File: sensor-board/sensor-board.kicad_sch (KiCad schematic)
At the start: 7 parts, among them U1 NE5532

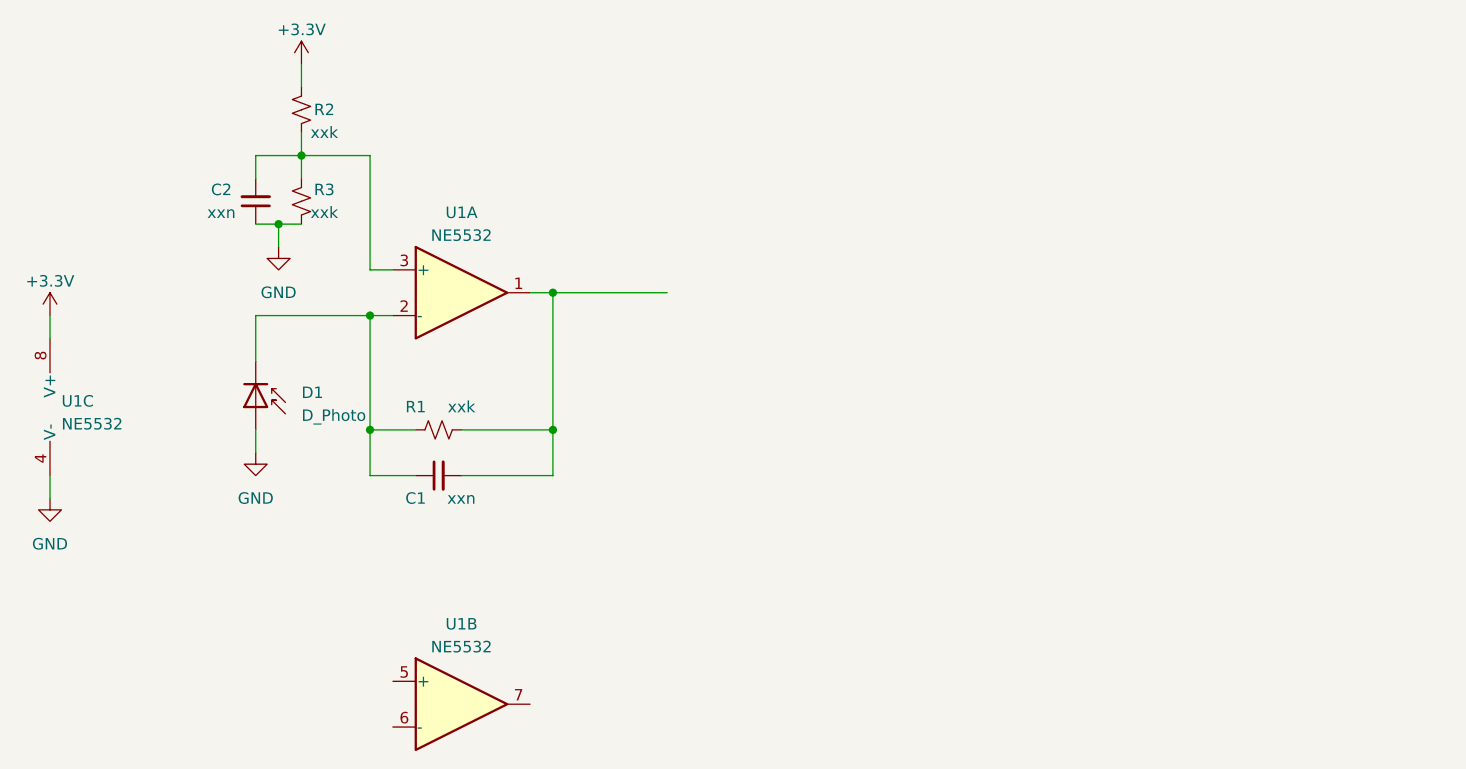
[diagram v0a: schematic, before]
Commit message: Updated sensor board
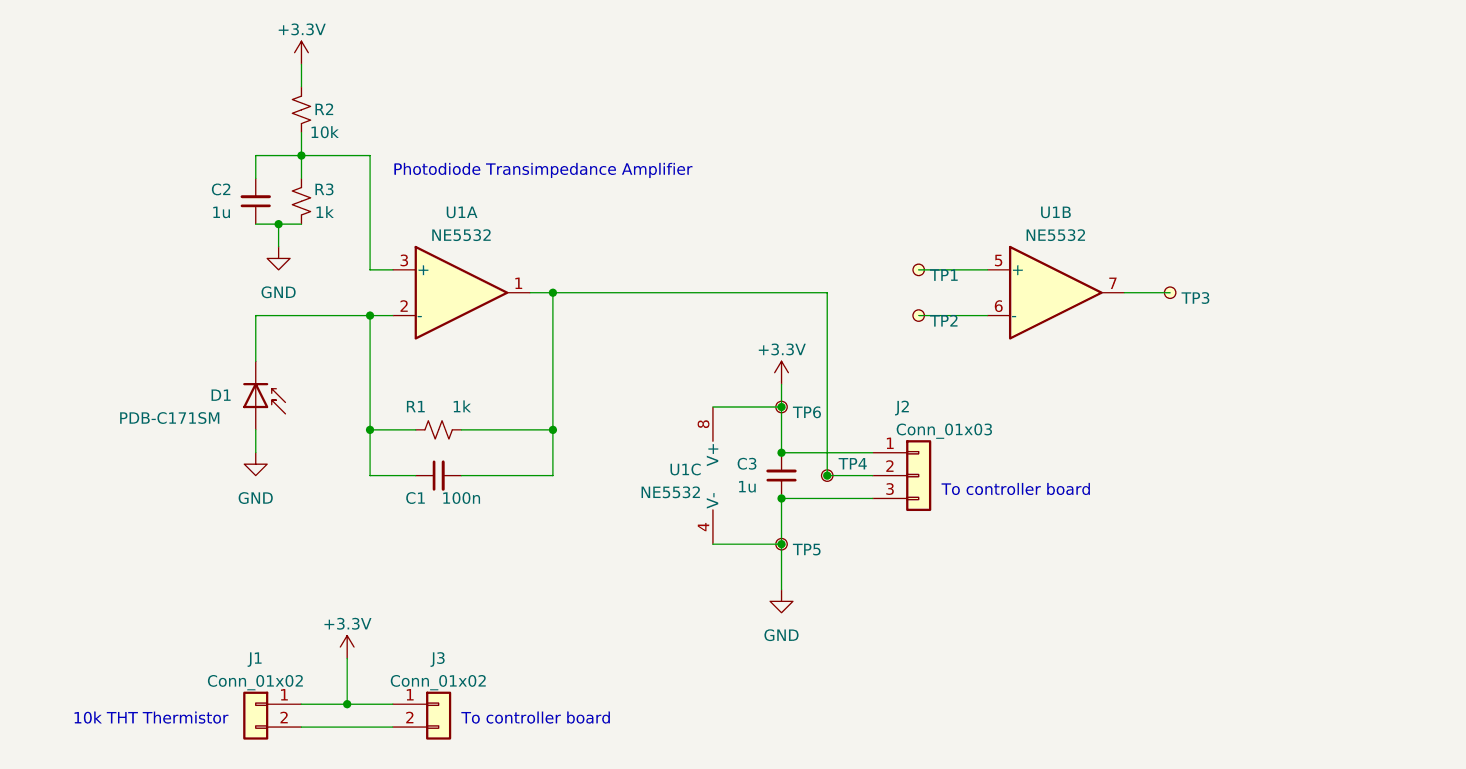
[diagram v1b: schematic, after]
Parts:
- added C3: 1u, Capacitor_SMD:C_0603_1608Metric, symbol Device:C_Small
- added J1, J3: Conn_01x02, Connector_PinHeader_2.54mm:PinHeader_1x02_P2.54mm_Vertical, symbol Connector_Generic:Conn_01x02
- added J2: Conn_01x03, Connector_PinHeader_2.54mm:PinHeader_1x03_P2.54mm_Vertical, symbol Connector_Generic:Conn_01x03
- added TP1, TP2, TP3, TP4, TP5, TP6: TestPoint-MinTH, oresat-misc:TestPoint-MinTH, symbol oresat-misc:TestPoint-MinTH
- C1: value xxn -> 100n; footprint (none) -> Capacitor_SMD:C_0603_1608Metric
- C2: value xxn -> 1u; footprint (none) -> Capacitor_SMD:C_0603_1608Metric
- D1: value D_Photo -> PDB-C171SM; footprint (none) -> oresat-diodes:PDB-C171
- R1, R3: value xxk -> 1k; footprint (none) -> Resistor_SMD:R_0603_1608Metric
- R2: value xxk -> 10k; footprint (none) -> Resistor_SMD:R_0603_1608Metric
- U1: footprint (none) -> Package_SO:SOIC-8_3.9x4.9mm_P1.27mm
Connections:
- net +3.3V: now also C3.2, J1.1 (Pin_1), J2.1 (Pin_1), J3.1 (Pin_1), TP6.1
- net GND: now also C3.1, J2.3 (Pin_3), TP5.1
- net at C1.2, R1.2, U1.1: now also J2.2 (Pin_2), TP4.1
- net at U1.5 (+): now also TP1.1
- net at U1.6 (-): now also TP2.1
- net at U1.7: now also TP3.1
- new net: J1.2 (Pin_2), J3.2 (Pin_2)
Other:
- note added: "10k THT Thermistor"
- note added: "Photodiode Transimpedance Amplifier"
- note added: "To controller board"
- moved on the sheet: U1B, U1C

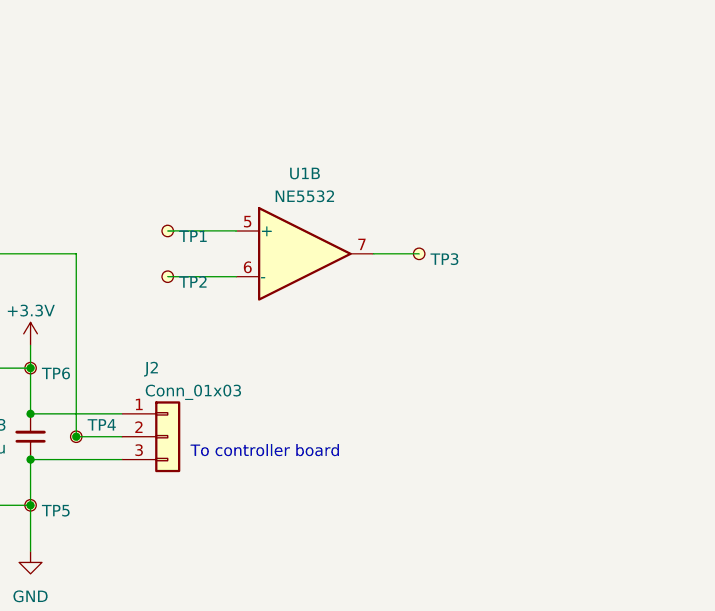
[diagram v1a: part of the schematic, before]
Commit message: Added 0 ohms to U1B inputs
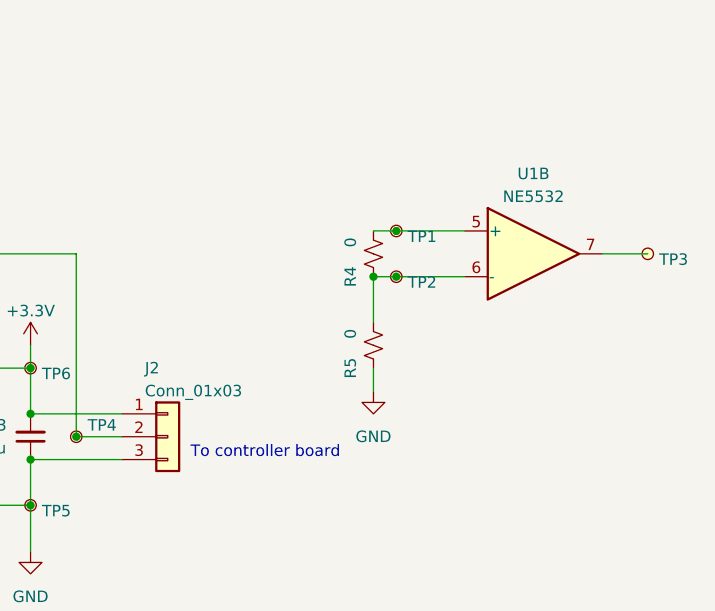
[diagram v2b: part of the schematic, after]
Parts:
- added R4, R5: 0, Resistor_SMD:R_0603_1608Metric, symbol Device:R_Small_US
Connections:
- net GND: now also R5.1
- net at TP1.1, U1.5 (+): now also R4.2
- net at TP2.1, U1.6 (-): now also R4.1, R5.2
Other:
- moved on the sheet: TP1, TP2, TP3, U1B
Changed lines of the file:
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@@
 (kicad_sch (version 20230121) (generator eeschema)
   (paper "A4")
+  (junction (at 193.04 66.04) (diameter 0) (color 0 0 0 0)
+  )
   (junction (at 109.22 66.04) (diameter 0) (color 0 0 0 0)
   )
@@
   (junction (at 154.94 86.36) (diameter 0) (color 0 0 0 0)
   )
+  (junction (at 195.58 66.04) (diameter 0) (color 0 0 0 0)
+  )
   (junction (at 129.54 63.5) (diameter 0) (color 0 0 0 0)
   )
   (junction (at 154.94 91.44) (diameter 0) (color 0 0 0 0)
   )
+  (junction (at 195.58 60.96) (diameter 0) (color 0 0 0 0)
+  )
   (junction (at 109.22 78.74) (diameter 0) (color 0 0 0 0)
   )
@@
     (stroke (width 0) (type default))
   )
-  (wire (pts (xy 170.18 60.96) (xy 177.8 60.96))
-    (stroke (width 0) (type default))
-  )
-  (wire (pts (xy 170.18 66.04) (xy 177.8 66.04))
-    (stroke (width 0) (type default))
-  )
-  (wire (pts (xy 193.04 63.5) (xy 198.12 63.5))
+  (wire (pts (xy 195.58 60.96) (xy 203.2 60.96))
+    (stroke (width 0) (type default))
+  )
+  (wire (pts (xy 195.58 66.04) (xy 203.2 66.04))
+    (stroke (width 0) (type default))
+  )
+  (wire (pts (xy 218.44 63.5) (xy 223.52 63.5))
     (stroke (width 0) (type default))
   )
@@
     (stroke (width 0) (type default))
   )
+  (wire (pts (xy 193.04 60.96) (xy 195.58 60.96))
+    (stroke (width 0) (type default))
+  )
   (wire (pts (xy 101.6 48.26) (xy 101.6 50.8))
     (stroke (width 0) (type default))
@@
     (stroke (width 0) (type default))
   )
+  (wire (pts (xy 193.04 66.04) (xy 193.04 71.12))
+    (stroke (width 0) (type default))
+  )
   (wire (pts (xy 109.22 60.96) (xy 111.76 60.96))
     (stroke (width 0) (type default))
@@
     (stroke (width 0) (type default))
   )
+  (wire (pts (xy 193.04 66.04) (xy 195.58 66.04))
+    (stroke (width 0) (type default))
+  )
   (wire (pts (xy 160.02 83.82) (xy 160.02 63.5))
     (stroke (width 0) (type default))
@@
   )
   (wire (pts (xy 96.52 66.04) (xy 109.22 66.04))
+    (stroke (width 0) (type default))
+  )
+  (wire (pts (xy 193.04 76.2) (xy 193.04 78.74))
     (stroke (width 0) (type default))
   )
@@
     )
   )
-  (symbol (lib_id "Amplifier_Operational:NE5532") (at 185.42 63.5 0) (unit 2)
-    (in_bom yes) (on_board yes) (dnp no) (fields_autoplaced)
-    (property "Reference" "U1" (at 185.42 54.61 0)
-      (effects (font (size 1.27 1.27)))
-    )
-    (property "Value" "NE5532" (at 185.42 57.15 0)
-      (effects (font (size 1.27 1.27)))
-    )
-    (property "Footprint" "Package_SO:SOIC-8_3.9x4.9mm_P1.27mm" (at 185.42 63.5 0)
-      (effects (font (size 1.27 1.27)) hide)
-    )
-    (property "Datasheet" "http://www.ti.com/lit/ds/symlink/ne5532.pdf" (at 185.42 63.5 0)
+  (symbol (lib_id "Amplifier_Operational:NE5532") (at 210.82 63.5 0) (unit 2)
+    (in_bom yes) (on_board yes) (dnp no) (fields_autoplaced)
+    (property "Reference" "U1" (at 210.82 54.61 0)
+      (effects (font (size 1.27 1.27)))
+    )
+    (property "Value" "NE5532" (at 210.82 57.15 0)
+      (effects (font (size 1.27 1.27)))
+    )
+    (property "Footprint" "Package_SO:SOIC-8_3.9x4.9mm_P1.27mm" (at 210.82 63.5 0)
+      (effects (font (size 1.27 1.27)) hide)
+    )
+    (property "Datasheet" "http://www.ti.com/lit/ds/symlink/ne5532.pdf" (at 210.82 63.5 0)
       (effects (font (size 1.27 1.27)) hide)
     )
@@
     )
   )
+  (symbol (lib_id "power:GND") (at 193.04 78.74 0) (unit 1)
+    (in_bom yes) (on_board yes) (dnp no) (fields_autoplaced)
+    (property "Reference" "#PWR03" (at 193.04 85.09 0)
+      (effects (font (size 1.27 1.27)) hide)
+    )
+    (property "Value" "GND" (at 193.04 83.82 0)
+      (effects (font (size 1.27 1.27)))
+    )
+    (property "Footprint" "" (at 193.04 78.74 0)
+      (effects (font (size 1.27 1.27)) hide)
+    )
+    (property "Datasheet" "" (at 193.04 78.74 0)
+      (effects (font (size 1.27 1.27)) hide)
+    )
+    (pin "1")
+    (instances
+      (project "sensor-board"
+        (path "/e4ca9097-2657-4a0c-a780-9bb5cfefa276"
+          (reference "#PWR03") (unit 1)
+        )
+      )
+    )
+  )
   (symbol (lib_id "Device:C_Small") (at 96.52 53.34 180) (unit 1)
     (in_bom yes) (on_board yes) (dnp no)
@@
     )
   )
-  (symbol (lib_id "oresat-misc:TestPoint-MinTH") (at 170.18 66.04 0) (unit 1)
-    (in_bom yes) (on_board yes) (dnp no) (fields_autoplaced)
-    (property "Reference" "TP2" (at 171.45 66.675 0)
+  (symbol (lib_id "oresat-misc:TestPoint-MinTH") (at 195.58 66.04 0) (unit 1)
+    (in_bom yes) (on_board yes) (dnp no) (fields_autoplaced)
+    (property "Reference" "TP2" (at 196.85 66.675 0)
       (effects (font (size 1.27 1.27)) (justify left))
     )
-    (property "Value" "TestPoint-MinTH" (at 170.18 59.055 0)
-      (effects (font (size 1.27 1.27)) hide)
-    )
-    (property "Footprint" "oresat-misc:TestPoint-MinTH" (at 170.18 60.96 0)
-      (effects (font (size 1.27 1.27)) hide)
-    )
-    (property "Datasheet" "" (at 170.18 66.04 0)
+    (property "Value" "TestPoint-MinTH" (at 195.58 59.055 0)
+      (effects (font (size 1.27 1.27)) hide)
+    )
+    (property "Footprint" "oresat-misc:TestPoint-MinTH" (at 195.58 60.96 0)
+      (effects (font (size 1.27 1.27)) hide)
+    )
+    (property "Datasheet" "" (at 195.58 66.04 0)
       (effects (font (size 1.27 1.27)) hide)
     )
@@
         (path "/e4ca9097-2657-4a0c-a780-9bb5cfefa276"
           (reference "R3") (unit 1)
+        )
+      )
+    )
+  )
+  (symbol (lib_id "Device:R_Small_US") (at 193.04 63.5 180) (unit 1)
+    (in_bom yes) (on_board yes) (dnp no)
+    (property "Reference" "R4" (at 190.5 66.04 90)
+      (effects (font (size 1.27 1.27)))
+    )
+    (property "Value" "0" (at 190.5 62.23 90)
+      (effects (font (size 1.27 1.27)))
+    )
+    (property "Footprint" "Resistor_SMD:R_0603_1608Metric" (at 193.04 63.5 0)
+      (effects (font (size 1.27 1.27)) hide)
+    )
+    (property "Datasheet" "~" (at 193.04 63.5 0)
+      (effects (font (size 1.27 1.27)) hide)
+    )
+    (pin "1")
+    (pin "2")
+    (instances
+      (project "sensor-board"
+        (path "/e4ca9097-2657-4a0c-a780-9bb5cfefa276"
+          (reference "R4") (unit 1)
         )
       )
@@
     )
   )
-  (symbol (lib_id "oresat-misc:TestPoint-MinTH") (at 198.12 63.5 0) (unit 1)
-    (in_bom yes) (on_board yes) (dnp no) (fields_autoplaced)
-    (property "Reference" "TP3" (at 199.39 64.135 0)
+  (symbol (lib_id "Device:R_Small_US") (at 193.04 73.66 180) (unit 1)
+    (in_bom yes) (on_board yes) (dnp no)
+    (property "Reference" "R5" (at 190.5 76.2 90)
+      (effects (font (size 1.27 1.27)))
+    )
+    (property "Value" "0" (at 190.5 72.39 90)
+      (effects (font (size 1.27 1.27)))
+    )
+    (property "Footprint" "Resistor_SMD:R_0603_1608Metric" (at 193.04 73.66 0)
+      (effects (font (size 1.27 1.27)) hide)
+    )
+    (property "Datasheet" "~" (at 193.04 73.66 0)
+      (effects (font (size 1.27 1.27)) hide)
+    )
+    (pin "1")
+    (pin "2")
+    (instances
+      (project "sensor-board"
+        (path "/e4ca9097-2657-4a0c-a780-9bb5cfefa276"
+          (reference "R5") (unit 1)
+        )
+      )
+    )
+  )
+  (symbol (lib_id "oresat-misc:TestPoint-MinTH") (at 223.52 63.5 0) (unit 1)
+    (in_bom yes) (on_board yes) (dnp no) (fields_autoplaced)
+    (property "Reference" "TP3" (at 224.79 64.135 0)
       (effects (font (size 1.27 1.27)) (justify left))
     )
-    (property "Value" "TestPoint-MinTH" (at 198.12 56.515 0)
-      (effects (font (size 1.27 1.27)) hide)
-    )
-    (property "Footprint" "oresat-misc:TestPoint-MinTH" (at 198.12 58.42 0)
-      (effects (font (size 1.27 1.27)) hide)
-    )
-    (property "Datasheet" "" (at 198.12 63.5 0)
+    (property "Value" "TestPoint-MinTH" (at 223.52 56.515 0)
+      (effects (font (size 1.27 1.27)) hide)
+    )
+    (property "Footprint" "oresat-misc:TestPoint-MinTH" (at 223.52 58.42 0)
+      (effects (font (size 1.27 1.27)) hide)
+    )
+    (property "Datasheet" "" (at 223.52 63.5 0)
       (effects (font (size 1.27 1.27)) hide)
     )
@@
     )
   )
-  (symbol (lib_id "oresat-misc:TestPoint-MinTH") (at 170.18 60.96 0) (unit 1)
-    (in_bom yes) (on_board yes) (dnp no) (fields_autoplaced)
-    (property "Reference" "TP1" (at 171.45 61.595 0)
+  (symbol (lib_id "oresat-misc:TestPoint-MinTH") (at 195.58 60.96 0) (unit 1)
+    (in_bom yes) (on_board yes) (dnp no) (fields_autoplaced)
+    (property "Reference" "TP1" (at 196.85 61.595 0)
       (effects (font (size 1.27 1.27)) (justify left))
     )
-    (property "Value" "TestPoint-MinTH" (at 170.18 53.975 0)
-      (effects (font (size 1.27 1.27)) hide)
-    )
-    (property "Footprint" "oresat-misc:TestPoint-MinTH" (at 170.18 55.88 0)
-      (effects (font (size 1.27 1.27)) hide)
-    )
-    (property "Datasheet" "" (at 170.18 60.96 0)
-      (effects (font (size 1.27 1.27)) hide)
-    )
+    (property "Value" "TestPoint-MinTH" (at 195.58 53.975 0)
+      (effects (font (size 1.27 1.27)) hide)
+    )
+    (property "Footprint" "oresat-misc:TestPoint-MinTH" (at 195.58 55.88 0)
+      (effects (font (size 1.27 1.27)) hide)
+    )
+    (property "Datasheet" "" (at 195.58 60.96 0)
+      (effects (font (size 1.27 1.27)) hide)
+    )
